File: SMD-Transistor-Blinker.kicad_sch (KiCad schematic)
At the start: 11 parts, among them J1 Conn_01x02_Pin, Q1 BC846, Q2 BC846

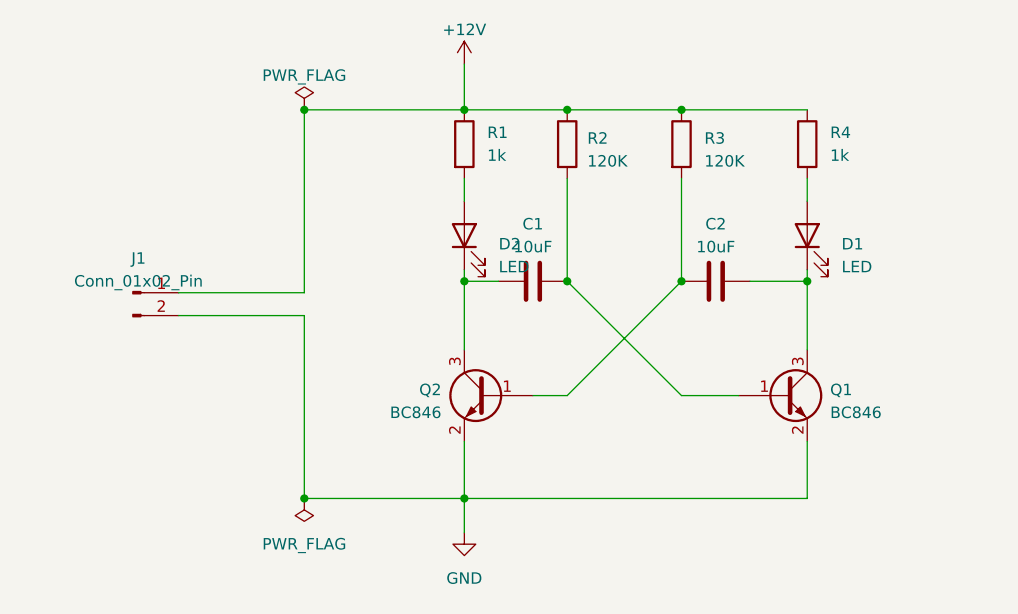
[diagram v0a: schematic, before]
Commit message: added additional ground pin
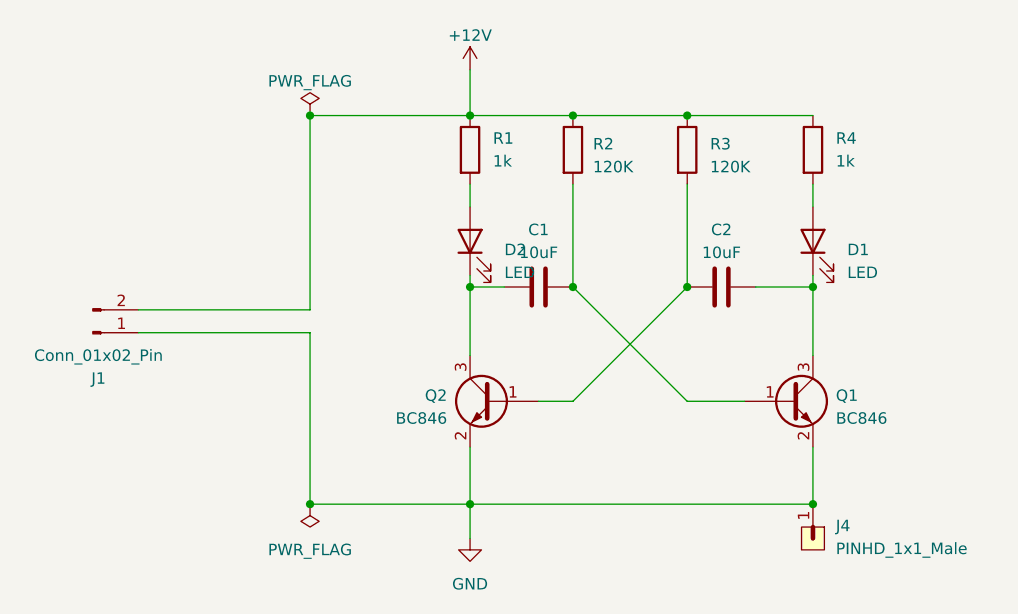
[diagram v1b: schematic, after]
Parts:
- added J4: PINHD_1x1_Male, Connector_PinHeader_2.54mm:PinHeader_1x01_P2.54mm_Vertical, symbol PCM_SL_Pin_Headers:PINHD_1x1_Male
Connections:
- net +12V: now also J1.2 (Pin_2); no longer J1.1 (Pin_1)
- net GND: now also J1.1 (Pin_1), J4.1; no longer J1.2 (Pin_2)
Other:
- moved on the sheet: C1, C2, D1, D2, J1, Q1, Q2, R1, R2, R3, R4
